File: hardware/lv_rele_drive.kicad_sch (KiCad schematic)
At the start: 0 parts

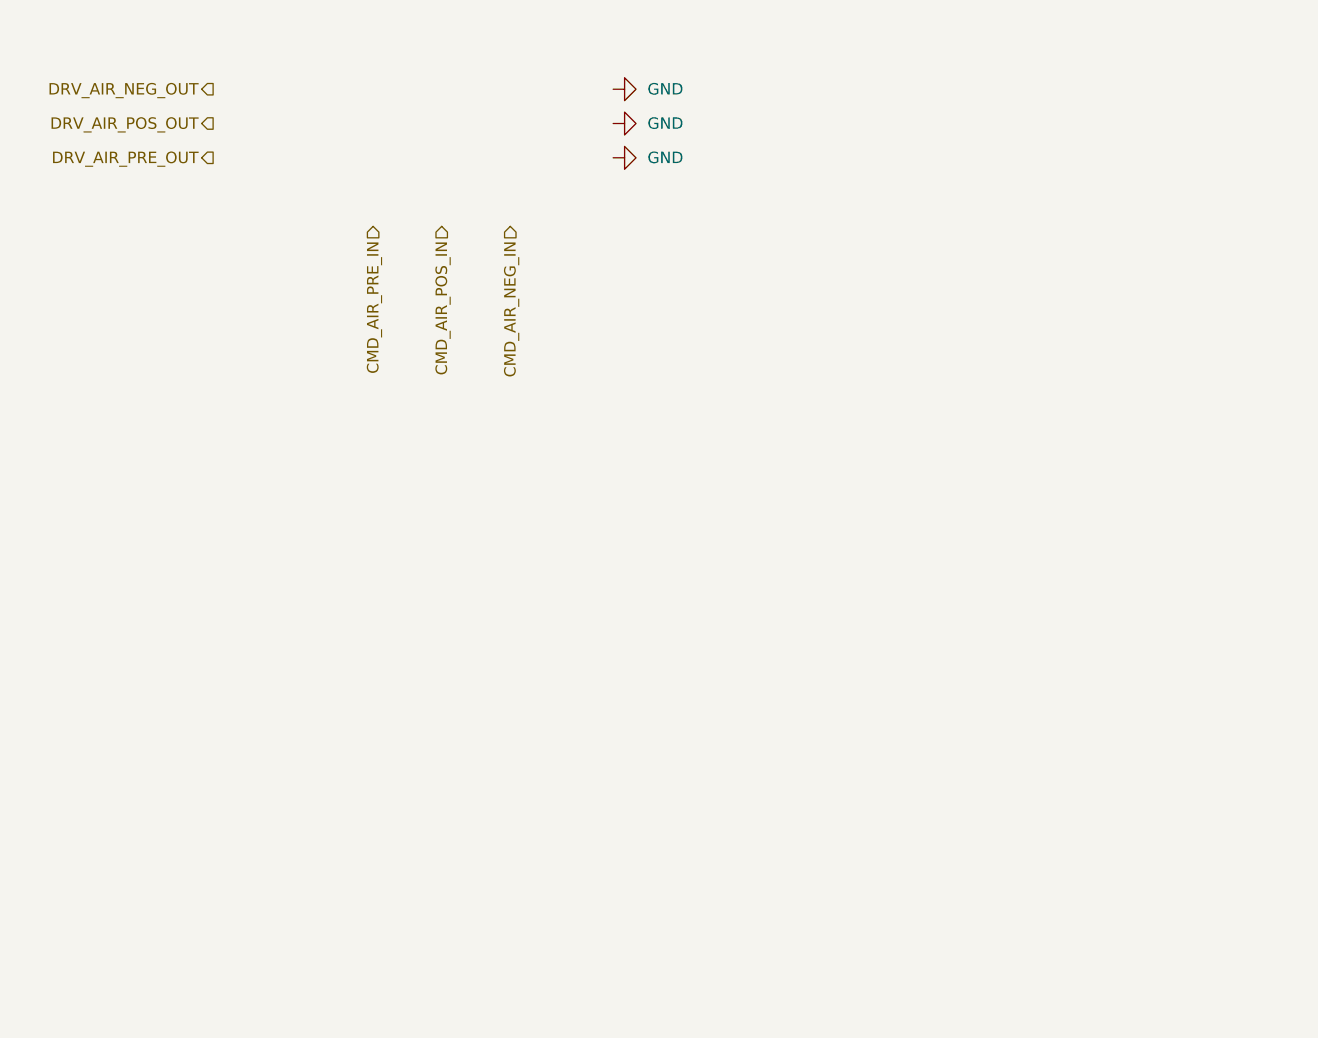
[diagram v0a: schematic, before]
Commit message: add rele drive to rele drive block
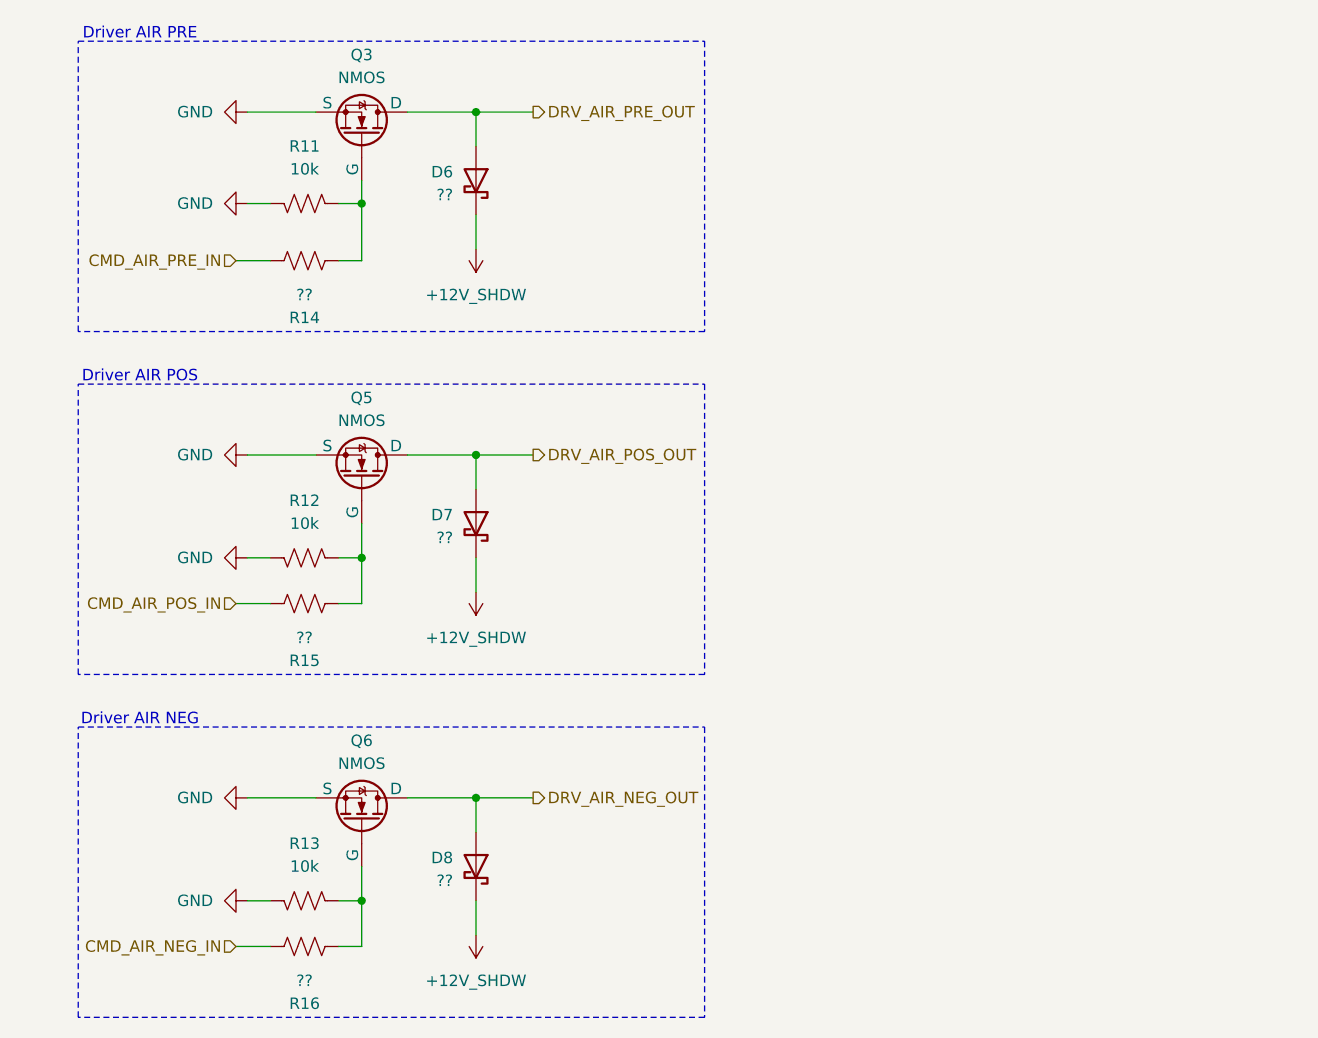
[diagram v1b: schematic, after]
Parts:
- added D6, D7, D8: ??, symbol Device:D_Schottky
- added Q3, Q5, Q6: NMOS, symbol Simulation_SPICE:NMOS
- added R11, R12, R13: 10k, symbol Device:R_US
- added R14, R15, R16: ??, symbol Device:R_US
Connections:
- net CMD_AIR_NEG_IN: now also R16.2
- net CMD_AIR_POS_IN: now also R15.2
- net CMD_AIR_PRE_IN: now also R14.2
- net DRV_AIR_NEG_OUT: now also D8.2 (A), Q6.1 (D)
- net DRV_AIR_POS_OUT: now also D7.2 (A), Q5.1 (D)
- net DRV_AIR_PRE_OUT: now also D6.2 (A), Q3.1 (D)
- net GND: now also Q3.3 (S), Q5.3 (S), Q6.3 (S), R11.2, R12.2, R13.2
- new net: Q3.2 (G), R11.1, R14.1
- new net: Q5.2 (G), R12.1, R15.1
- new net: Q6.2 (G), R13.1, R16.1
- new net +12V_SHDW: D6.1 (K), D7.1 (K), D8.1 (K)
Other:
- note added: "Driver AIR NEG"
- note added: "Driver AIR POS"
- note added: "Driver AIR PRE"

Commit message: import relay package; add relays and precharge resistor to hv_power block; add flywheel protections to lv_relay_drive block
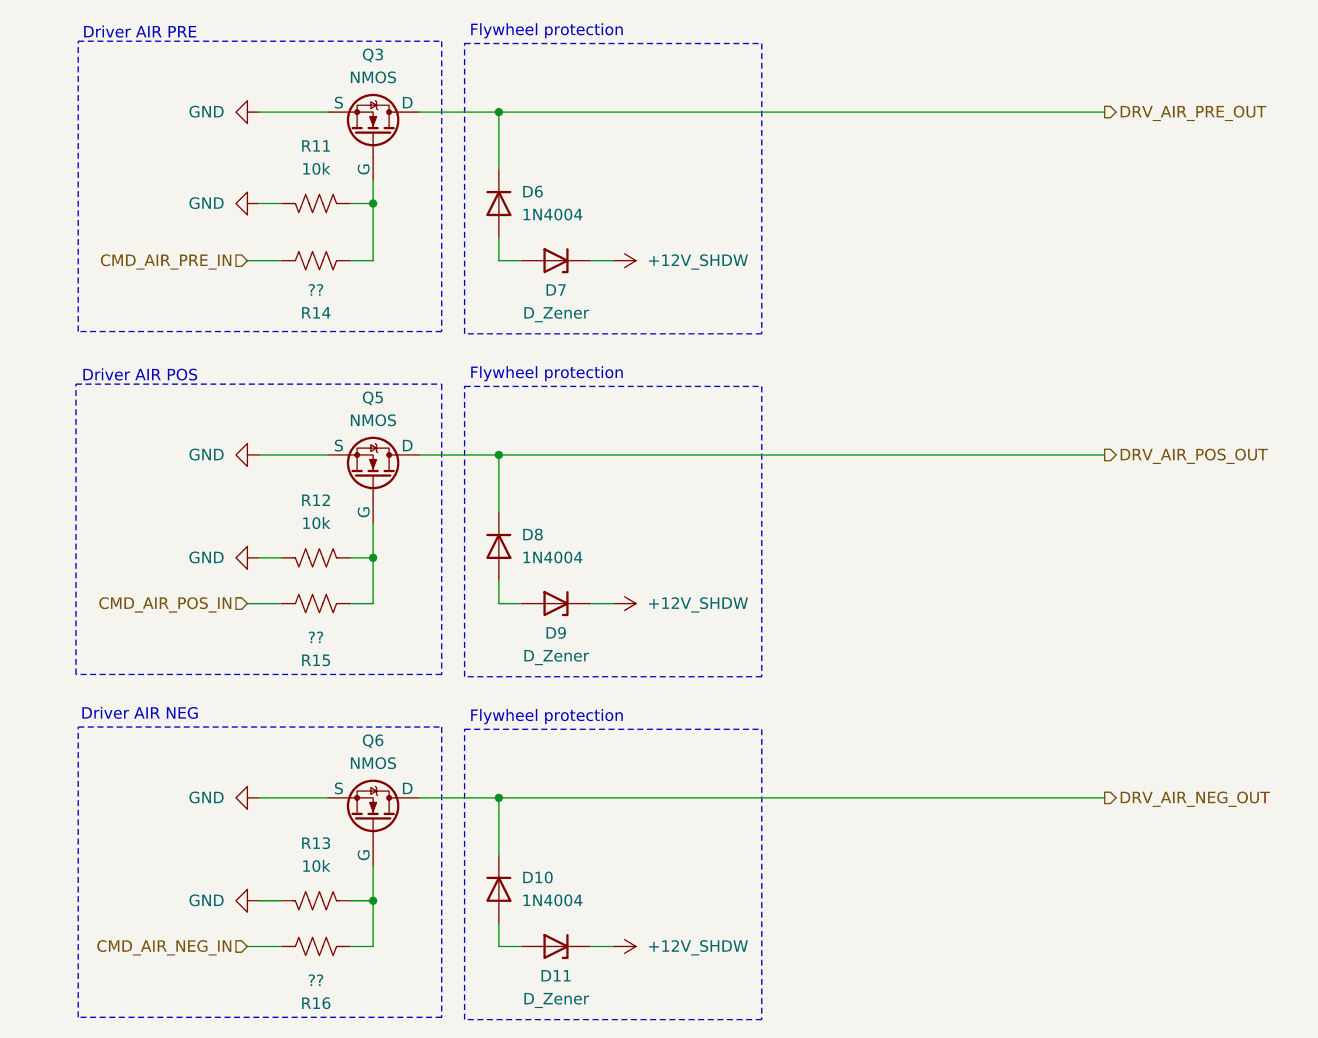
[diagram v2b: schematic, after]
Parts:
- removed D6, D7, D8: ??, symbol Device:D_Schottky
- added D10, D6, D8: 1N4004, Diode_THT:D_DO-41_SOD81_P10.16mm_Horizontal, symbol Diode:1N4004
- added D11, D7, D9: D_Zener, symbol Device:D_Zener
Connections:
- net +12V_SHDW: now also D11.1 (K), D7.1 (K), D9.1 (K)
- net DRV_AIR_NEG_OUT: now also D10.1 (K)
- net DRV_AIR_POS_OUT: now also D8.1 (K)
- net DRV_AIR_PRE_OUT: now also D6.1 (K)
- new net: D6.2 (A), D7.2 (A)
- new net: D10.2 (A), D11.2 (A)
- new net: D8.2 (A), D9.2 (A)
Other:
- note added: "Flywheel protection"
- moved on the sheet: Q3, Q5, Q6, R11, R12, R13, R14, R15, R16
